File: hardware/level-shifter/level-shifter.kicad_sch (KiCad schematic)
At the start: 28 parts, among them J1 Conn_01x10_Socket, J2 Conn_01x10_Socket, J3 Conn_01x10_Socket, J4 Conn_01x10_Socket, J5 Conn_01x10_Pin, J6 Conn_01x10_Pin, J7 Conn_01x10_Pin, J8 Conn_01x10_Pin

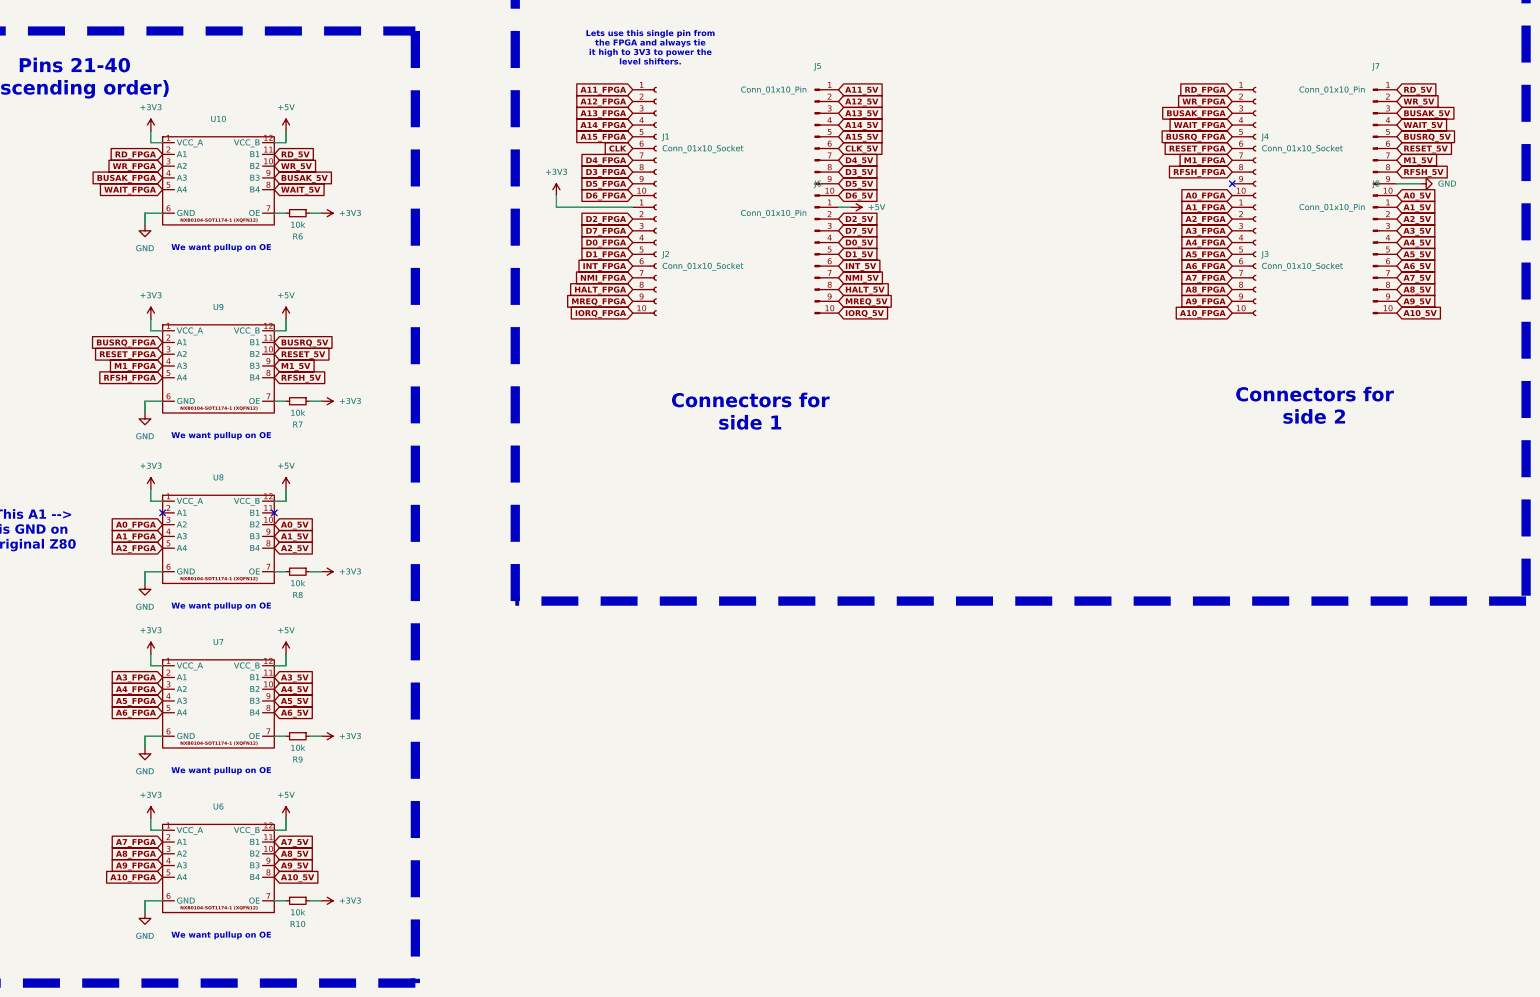
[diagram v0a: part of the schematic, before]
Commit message: level shifter redo
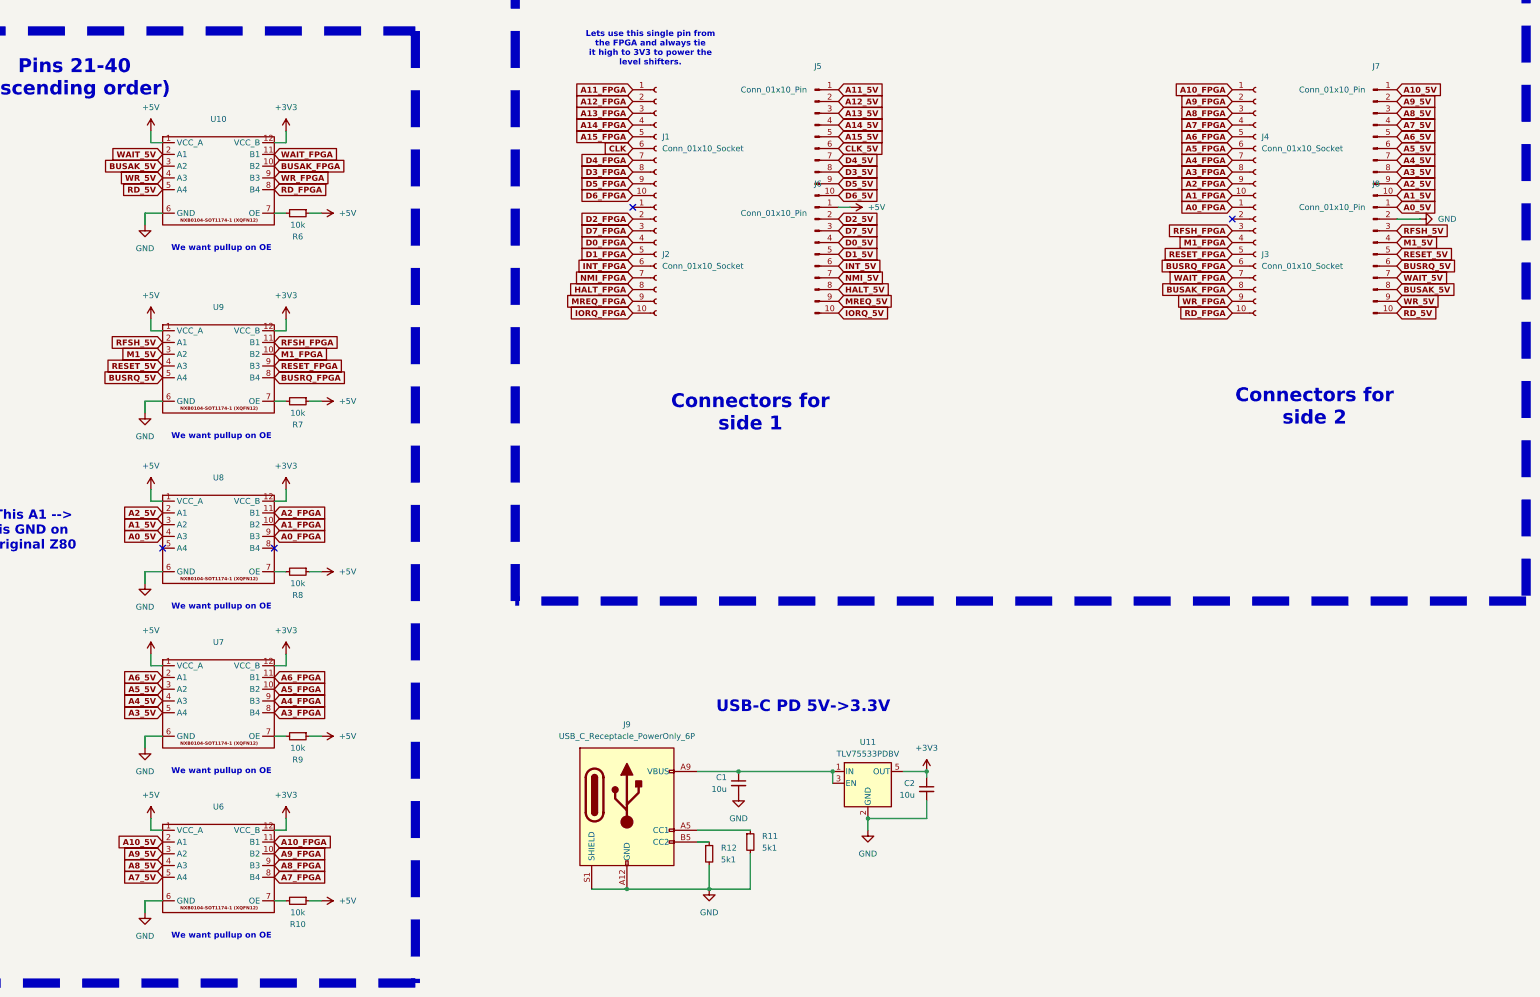
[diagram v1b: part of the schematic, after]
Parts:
- added C1, C2: 10u, Capacitor_SMD:C_0805_2012Metric_Pad1.18x1.45mm_HandSolder, symbol Device:C_Small
- added J9: USB_C_Receptacle_PowerOnly_6P, Connector_USB:USB_C_Receptacle_GCT_USB4125-xx-x_6P_TopMnt_Horizontal, symbol Connector:USB_C_Receptacle_PowerOnly_6P
- added R11, R12: 5k1, Resistor_SMD:R_0805_2012Metric_Pad1.20x1.40mm_HandSolder, symbol Device:R_Small
- added U11: TLV75533PDBV, Package_TO_SOT_SMD:SOT-23-5, symbol Regulator_Linear:TLV75533PDBV
- J1, J2, J3, J4: footprint Connector_PinSocket_2.54mm:PinSocket_1x10_P2.54mm_Vertical -> Connector_PinHeader_2.54mm:PinHeader_1x10_P2.54mm_Vertical; LCSC (none) -> C57369
- J5, J6, J7, J8: LCSC (none) -> C57369
- R1, R10, R2, R3, R4, R5, R6, R7, R8, R9: footprint Resistor_SMD:R_0201_0603Metric -> Resistor_SMD:R_0805_2012Metric_Pad1.20x1.40mm_HandSolder; LCSC (none) -> C17414
- U1, U10, U2, U3, U4, U5, U6, U7, U8, U9: LCSC (none) -> C551618
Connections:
- net +3V3: now also U10.12 (VCC_B), U6.12 (VCC_B), U7.12 (VCC_B), U8.12 (VCC_B), U9.12 (VCC_B), C2.1, U11.5 (OUT); no longer J2.1 (Pin_1), R10.1, R6.1, R7.1, R8.1, R9.1, U10.1 (VCC_A), U6.1 (VCC_A), U7.1 (VCC_A), U8.1 (VCC_A), U9.1 (VCC_A)
- net +5V: now also R10.1, R6.1, R7.1, R8.1, R9.1, U10.1 (VCC_A), U6.1 (VCC_A), U7.1 (VCC_A), U8.1 (VCC_A), U9.1 (VCC_A); no longer U10.12 (VCC_B), U6.12 (VCC_B), U7.12 (VCC_B), U8.12 (VCC_B), U9.12 (VCC_B)
- net A0_5V: now also J8.1 (Pin_1), U8.4 (A3); no longer J7.10 (Pin_10), U8.10 (B2)
- net A0_FPGA: now also J3.1 (Pin_1), U8.9 (B3); no longer J4.10 (Pin_10), U8.3 (A2)
- net A10_5V: now also J7.1 (Pin_1), U6.2 (A1); no longer J8.10 (Pin_10), U6.8 (B4)
- net A10_FPGA: now also J4.1 (Pin_1), U6.11 (B1); no longer J3.10 (Pin_10), U6.5 (A4)
- net A1_5V: now also J7.10 (Pin_10), U8.3 (A2); no longer J8.1 (Pin_1), U8.9 (B3)
- net A1_FPGA: now also J4.10 (Pin_10), U8.10 (B2); no longer J3.1 (Pin_1), U8.4 (A3)
- net A2_5V: now also J7.9 (Pin_9), U8.2 (A1); no longer J8.2 (Pin_2), U8.8 (B4)
- net A2_FPGA: now also J4.9 (Pin_9), U8.11 (B1); no longer J3.2 (Pin_2), U8.5 (A4)
- net A3_5V: now also J7.8 (Pin_8), U7.5 (A4); no longer J8.3 (Pin_3), U7.11 (B1)
- net A3_FPGA: now also J4.8 (Pin_8), U7.8 (B4); no longer J3.3 (Pin_3), U7.2 (A1)
- net A4_5V: now also J7.7 (Pin_7), U7.4 (A3); no longer J8.4 (Pin_4), U7.10 (B2)
- net A4_FPGA: now also J4.7 (Pin_7), U7.9 (B3); no longer J3.4 (Pin_4), U7.3 (A2)
- net A5_5V: now also J7.6 (Pin_6), U7.3 (A2); no longer J8.5 (Pin_5), U7.9 (B3)
- net A5_FPGA: now also J4.6 (Pin_6), U7.10 (B2); no longer J3.5 (Pin_5), U7.4 (A3)
- net A6_5V: now also J7.5 (Pin_5), U7.2 (A1); no longer J8.6 (Pin_6), U7.8 (B4)
- net A6_FPGA: now also J4.5 (Pin_5), U7.11 (B1); no longer J3.6 (Pin_6), U7.5 (A4)
- net A7_5V: now also J7.4 (Pin_4), U6.5 (A4); no longer J8.7 (Pin_7), U6.11 (B1)
- net A7_FPGA: now also J4.4 (Pin_4), U6.8 (B4); no longer J3.7 (Pin_7), U6.2 (A1)
- net A8_5V: now also J7.3 (Pin_3), U6.4 (A3); no longer J8.8 (Pin_8), U6.10 (B2)
- net A8_FPGA: now also J4.3 (Pin_3), U6.9 (B3); no longer J3.8 (Pin_8), U6.3 (A2)
- net A9_5V: now also J7.2 (Pin_2), U6.3 (A2); no longer J8.9 (Pin_9), U6.9 (B3)
- net A9_FPGA: now also J4.2 (Pin_2), U6.10 (B2); no longer J3.9 (Pin_9), U6.4 (A3)
- net BUSAK_5V: now also J8.8 (Pin_8), U10.3 (A2); no longer J7.3 (Pin_3), U10.9 (B3)
- net BUSAK_FPGA: now also J3.8 (Pin_8), U10.10 (B2); no longer J4.3 (Pin_3), U10.4 (A3)
- net BUSRQ_5V: now also J8.6 (Pin_6), U9.5 (A4); no longer J7.5 (Pin_5), U9.11 (B1)
- net BUSRQ_FPGA: now also J3.6 (Pin_6), U9.8 (B4); no longer J4.5 (Pin_5), U9.2 (A1)
- net GND: now also J8.2 (Pin_2), C1.2, C2.2, J9.A12 (GND), J9.B12 (GND), J9.S1 (SHIELD), R11.2, R12.2, U11.2 (GND); no longer J7.9 (Pin_9)
- net M1_5V: now also J8.4 (Pin_4), U9.3 (A2); no longer J7.7 (Pin_7), U9.9 (B3)
- net M1_FPGA: now also J3.4 (Pin_4), U9.10 (B2); no longer J4.7 (Pin_7), U9.4 (A3)
- net RD_5V: now also J8.10 (Pin_10), U10.5 (A4); no longer J7.1 (Pin_1), U10.11 (B1)
- net RD_FPGA: now also J3.10 (Pin_10), U10.8 (B4); no longer J4.1 (Pin_1), U10.2 (A1)
- net RESET_5V: now also J8.5 (Pin_5), U9.4 (A3); no longer J7.6 (Pin_6), U9.10 (B2)
- net RESET_FPGA: now also J3.5 (Pin_5), U9.9 (B3); no longer J4.6 (Pin_6), U9.3 (A2)
- net RFSH_5V: now also J8.3 (Pin_3), U9.2 (A1); no longer J7.8 (Pin_8), U9.8 (B4)
- net RFSH_FPGA: now also J3.3 (Pin_3), U9.11 (B1); no longer J4.8 (Pin_8), U9.5 (A4)
- net WAIT_5V: now also J8.7 (Pin_7), U10.2 (A1); no longer J7.4 (Pin_4), U10.8 (B4)
- net WAIT_FPGA: now also J3.7 (Pin_7), U10.11 (B1); no longer J4.4 (Pin_4), U10.5 (A4)
- net WR_5V: now also J8.9 (Pin_9), U10.4 (A3); no longer J7.2 (Pin_2), U10.10 (B2)
- net WR_FPGA: now also J3.9 (Pin_9), U10.9 (B3); no longer J4.2 (Pin_2), U10.3 (A2)
- new net: J9.A5 (CC1), R11.1
- new net: C1.1, J9.A9 (VBUS), J9.B9 (VBUS), U11.1 (IN), U11.3 (EN)
- new net: J9.B5 (CC2), R12.1
- no-connect marks 5 -> 6
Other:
- note added: "USB-C PD 5V->3.3V"

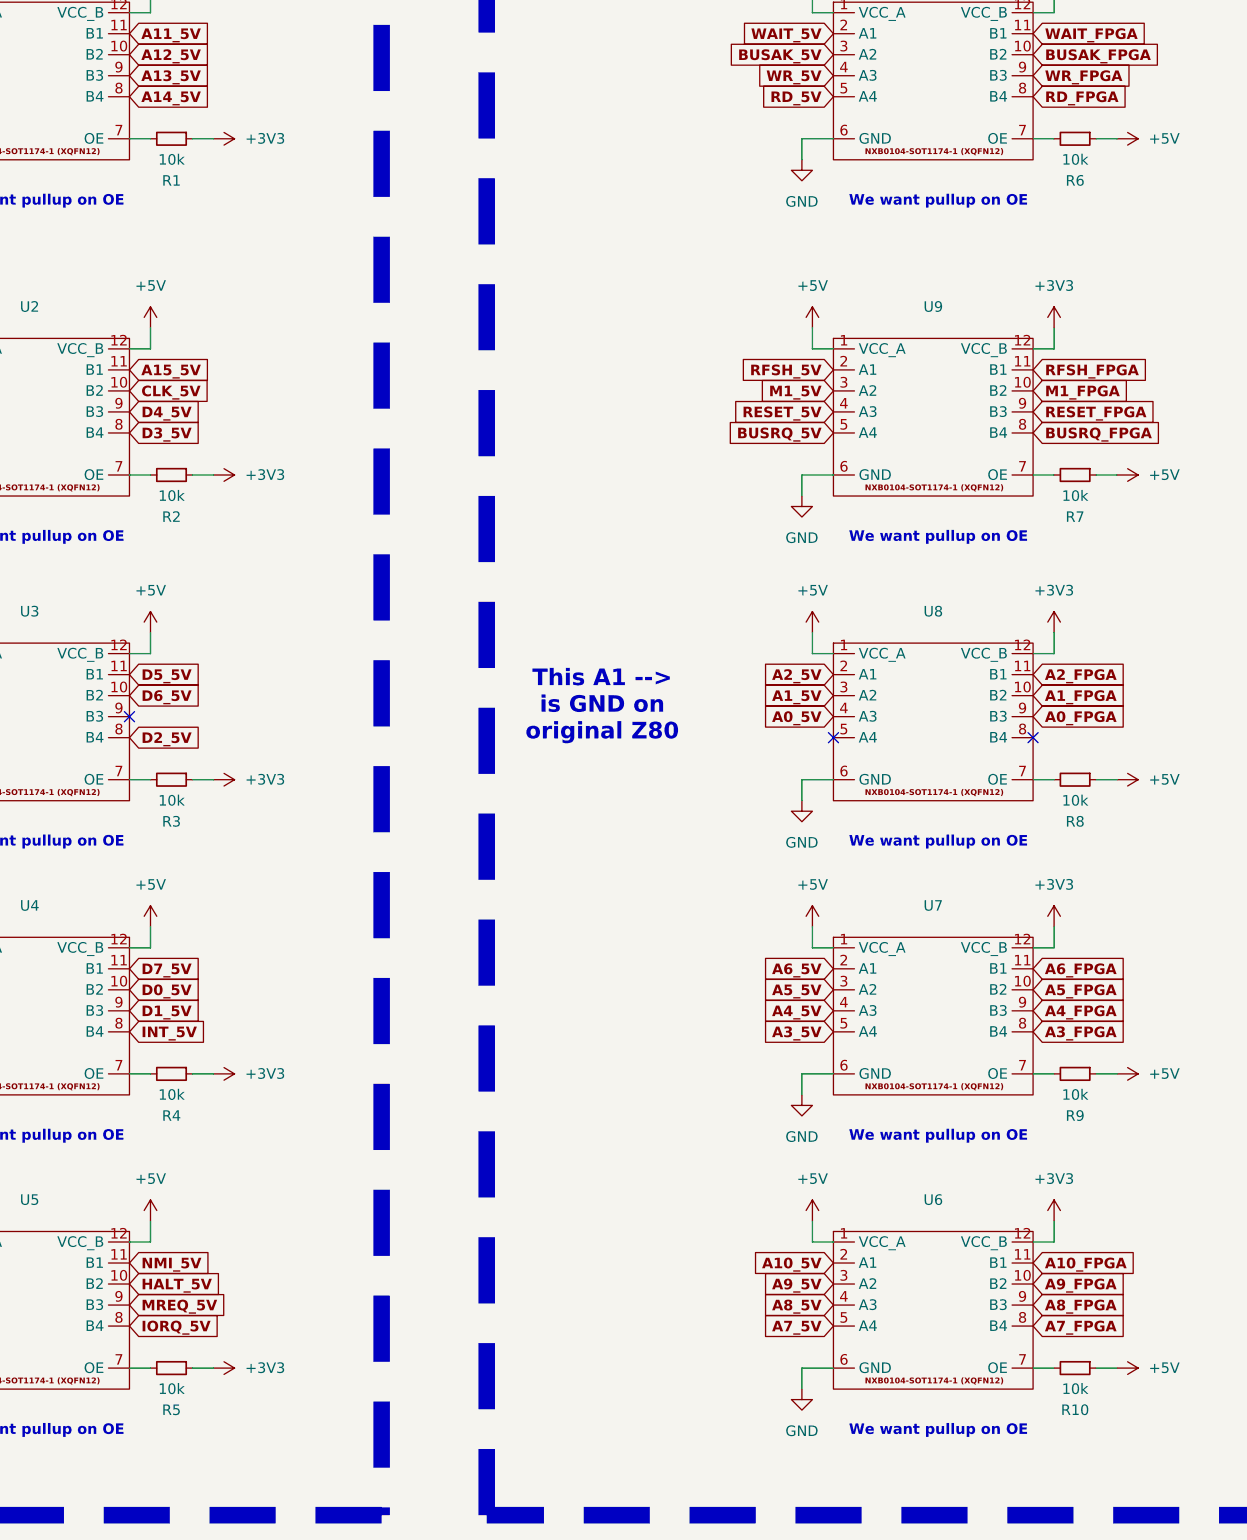
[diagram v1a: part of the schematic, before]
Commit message: remove old files from level shifter proj, add MPN for macrofab possible assembly
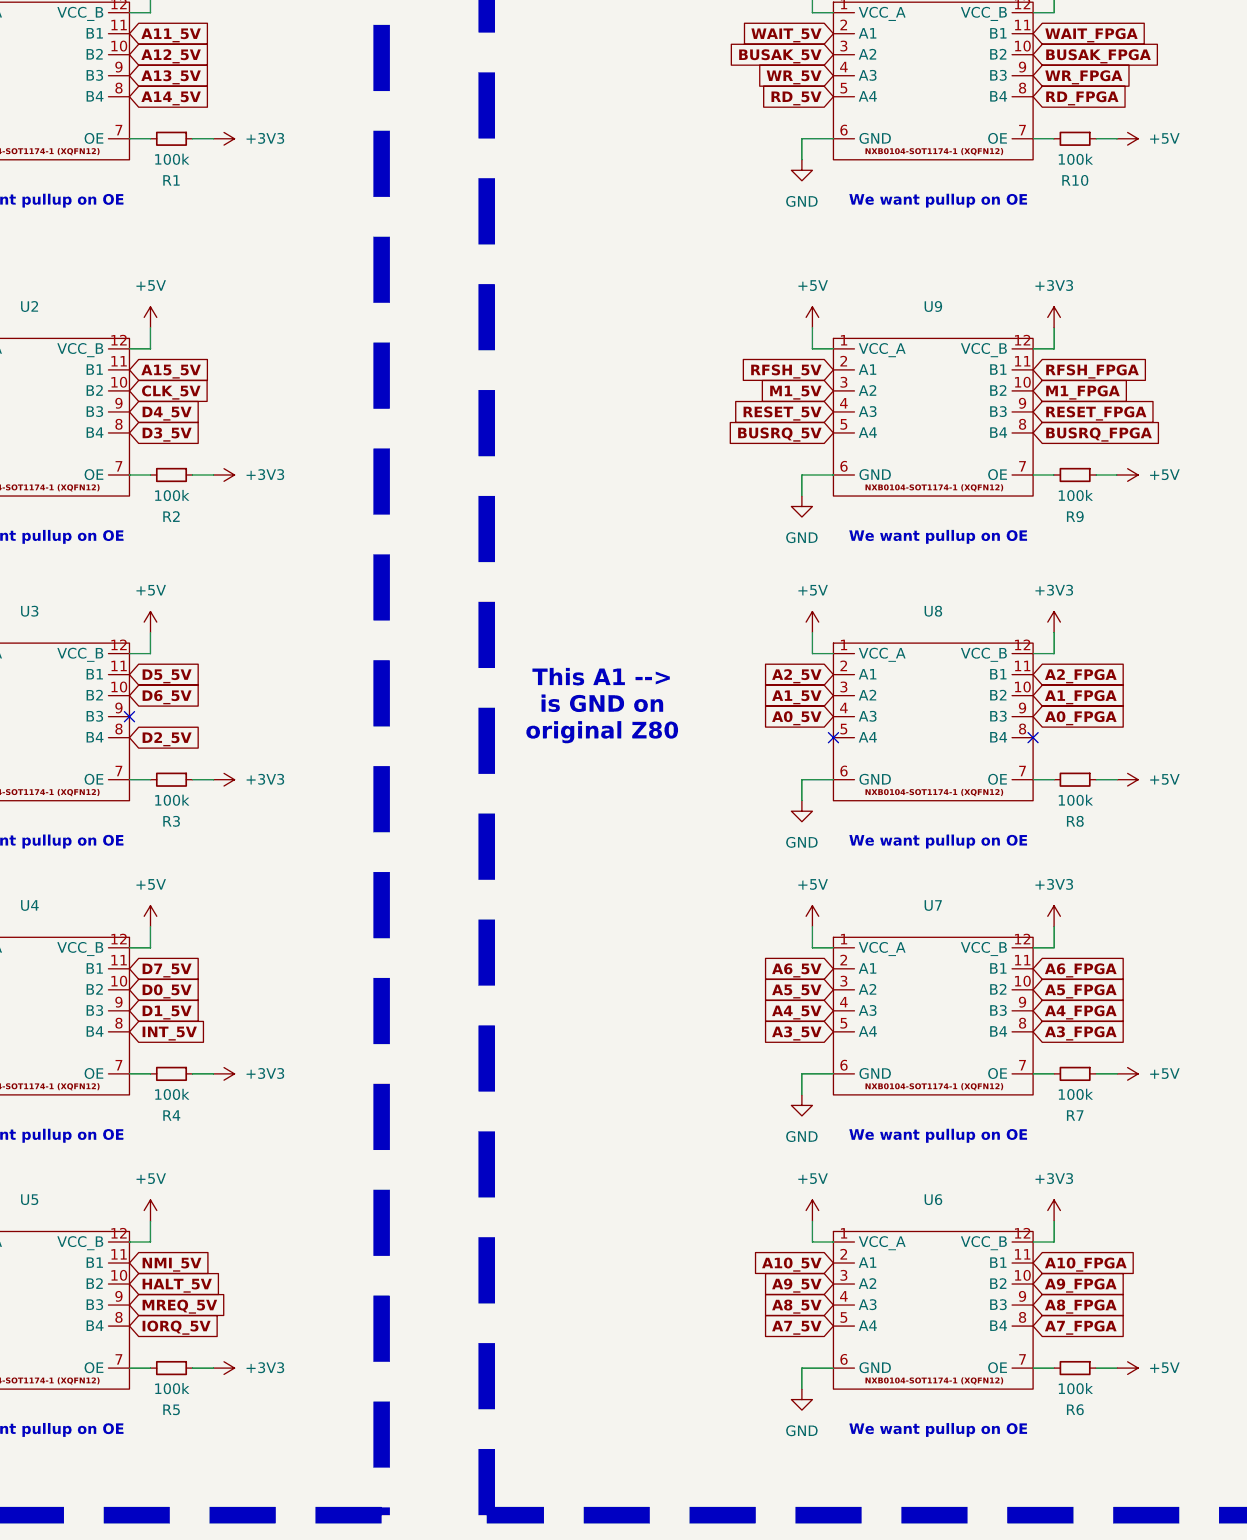
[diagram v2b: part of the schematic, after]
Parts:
- R1, R10, R2, R3, R4, R5, R6, R7, R8, R9: value 10k -> 100k; LCSC C17414 -> (none); MPN (none) -> ERJ-UP6D6202V
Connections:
- net at U9.7 (OE): now also R9.2; no longer R7.2
- net at U10.7 (OE): now also R10.2; no longer R6.2
- net at U6.7 (OE): now also R6.2; no longer R10.2
- net at U7.7 (OE): now also R7.2; no longer R9.2

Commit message: use marco USB header and filtering, add MPNs, via stitching for power planes
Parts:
- removed J9: USB_C_Receptacle_PowerOnly_6P, Connector_USB:USB_C_Receptacle_GCT_USB4125-xx-x_6P_TopMnt_Horizontal, symbol Connector:USB_C_Receptacle_PowerOnly_6P
- added C3, C4: 100n 20V, Capacitor_SMD:C_0805_2012Metric, symbol Device:C_Small
- added C5: 100n 16V, Capacitor_SMD:C_0603_1608Metric, symbol Device:C_Small
- added C6: 1u 10V, Capacitor_SMD:C_0805_2012Metric, symbol Device:C_Small
- added C7: 10u 10V, Capacitor_SMD:C_0603_1608Metric, symbol Device:C_Small
- added C8: 10u >= 5V, Capacitor_SMD:C_0603_1608Metric, symbol Device:C_Small
- added FB1: 25% 220 2.2A, Capacitor_SMD:C_0603_1608Metric, symbol Device:FerriteBead_Small
- added J9: USB_C_Receptacle_USB2.0_16P, Connector_USB:USB_C_Receptacle_GCT_USB4110, symbol Connector:USB_C_Receptacle_USB2.0_16P
- C1, C2: value 10u -> 10u 10V; footprint Capacitor_SMD:C_0805_2012Metric_Pad1.18x1.45mm_HandSolder -> Capacitor_SMD:C_0603_1608Metric; LCSC C1713 -> (none); MPN (none) -> CGA3EDX7T1A106M080AU
- R1, R10, R2, R3, R4, R5, R6, R7, R8, R9: footprint Resistor_SMD:R_0805_2012Metric_Pad1.20x1.40mm_HandSolder -> Resistor_SMD:R_0805_2012Metric
- R11, R12: value 5k1 -> 1% 5.1k 0.063W; footprint Resistor_SMD:R_0805_2012Metric_Pad1.20x1.40mm_HandSolder -> Resistor_SMD:R_0402_1005Metric; LCSC C26023 -> (none); MPN (none) -> CRCW04025K10FKED
- U11: LCSC C404027 -> (none)
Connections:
- net +3V3: now also C8.1; no longer C2.1
- net +5V: now also U11.1 (IN), U11.3 (EN), C5.1, C6.1, C7.1, FB1.2
- net GND: now also C3.2, C4.2, C5.2, C6.2, C7.2, C8.2, J9.A1 (GND), J9.A12 (GND), J9.B1 (GND), J9.B12 (GND), J9.S1 (SHIELD)
- net at R11.1: now also J9.A5 (CC1)
- net at R12.1: now also J9.B5 (CC2)
- new net: C1.1, C2.1, C3.1, C4.1, FB1.1, J9.A4 (VBUS), J9.A9 (VBUS), J9.B4 (VBUS), J9.B9 (VBUS)
- no-connect marks 6 -> 12
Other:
- note added: "Ferrite bead 0603"
- note added: "Pins 21-40 level-shifter sides flipped from 1-20 to make layout not painful"
- note added: "USB-C 5V->3V3 Power Supply from host PC"
- note added: "Z80 System <-> Translation Board Connectors"
- note added: "https://www.mouser.com/datasheet/2/916/NXB0104_Q100-1664477.pdf Level shifters 5V<->3V3 We are using the XQFN12 package OE pullup is referenced to VCC_A, >= 50k MacroFab MPNs specified"
- note removed: "Pins 21-40 (ascending order)"
- note removed: "USB-C PD 5V->3.3V"
- note removed: "https://www.mouser.com/datasheet/2/916/NXB0104_Q100-1664477.pdf Level shifters 5V<->3V3 We are using the XQFN12 package Search for kicad symbol "xqfn" OE is referenced to VCC_A"
